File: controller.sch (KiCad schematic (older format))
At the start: 22 parts, among them J1 Conn_01x16, J2 Conn_01x08, J3 Conn_01x04, SW1 SW_Push, U1 PRTR5V0U2X, U2 AT90USB1286-AU, Y1 16MHz

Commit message: Rescue symbol
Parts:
- U2: symbol MCU_Microchip_AVR:AT90USB1286-AU -> controller-rescue:AT90USB1286-AU-MCU_Microchip_AVR
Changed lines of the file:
@@
 EESchema Schematic File Version 4
-LIBS:controller-cache
 EELAYER 30 0
 EELAYER END
@@
 	9700 4850 9500 4850
 $Comp
-L MCU_Microchip_AVR:AT90USB1286-AU U2
+L controller-rescue:AT90USB1286-AU-MCU_Microchip_AVR U2
 U 1 1 5DC2549C
 P 6750 3500

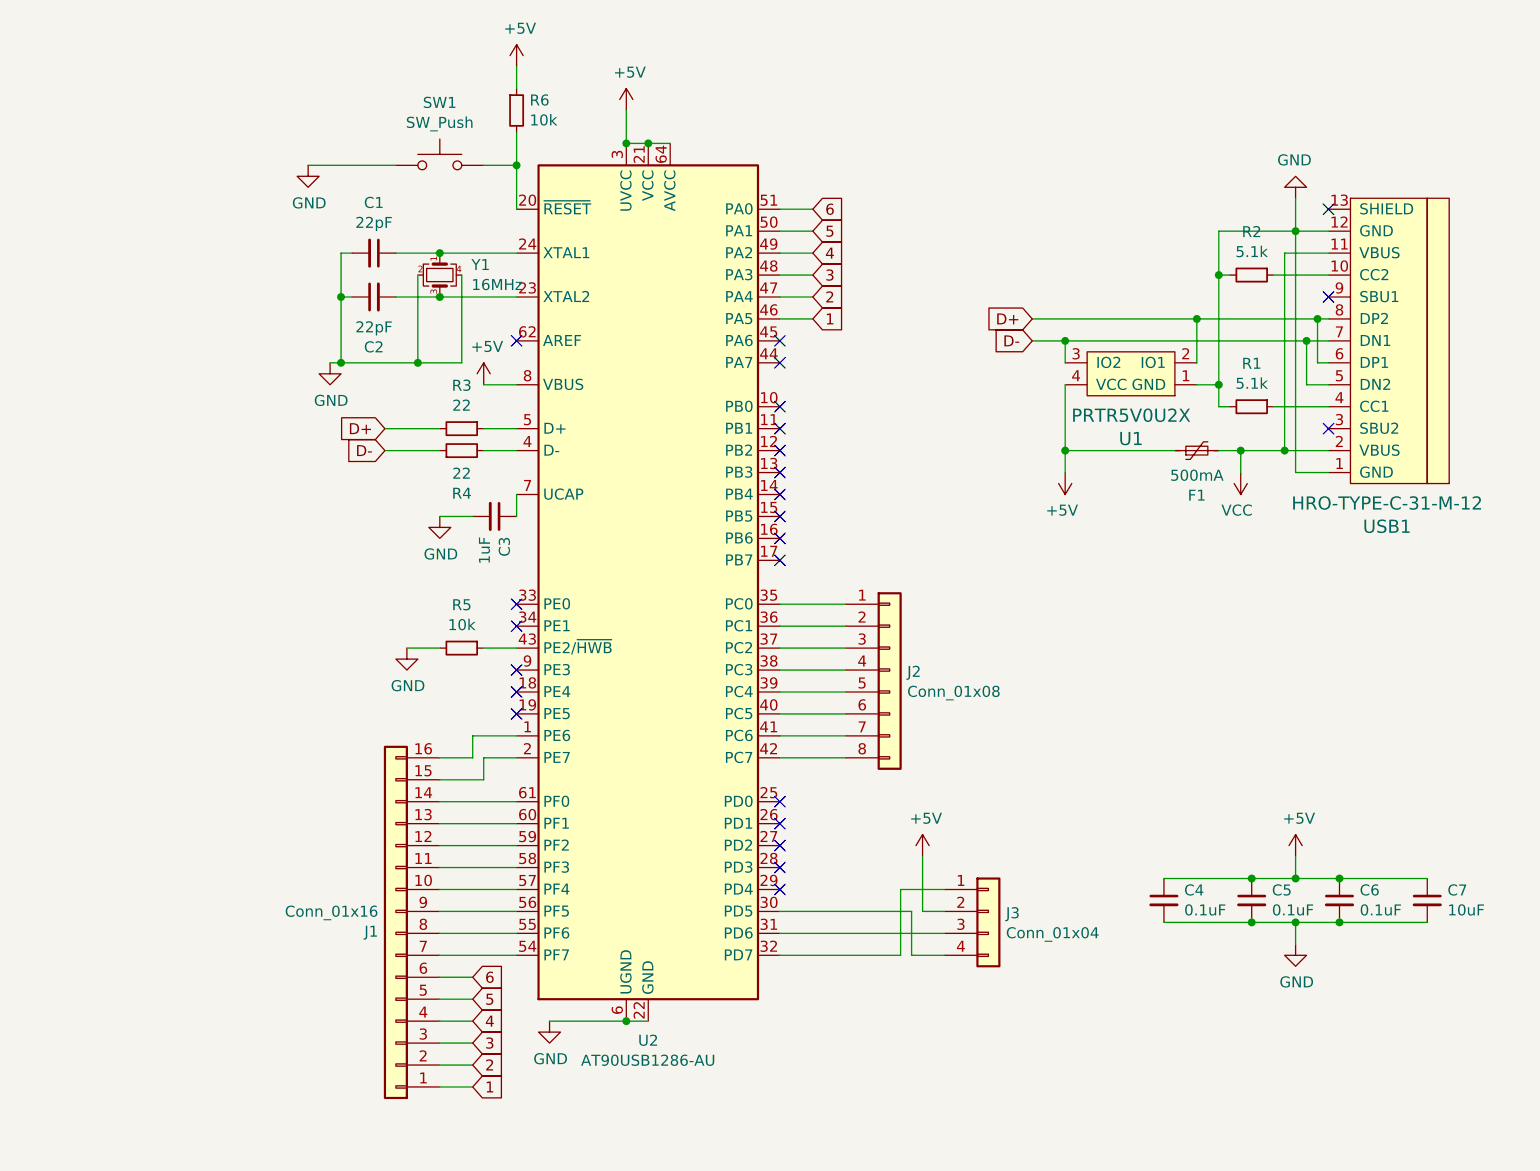
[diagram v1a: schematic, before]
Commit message: Schematic: add/delete/move connectors
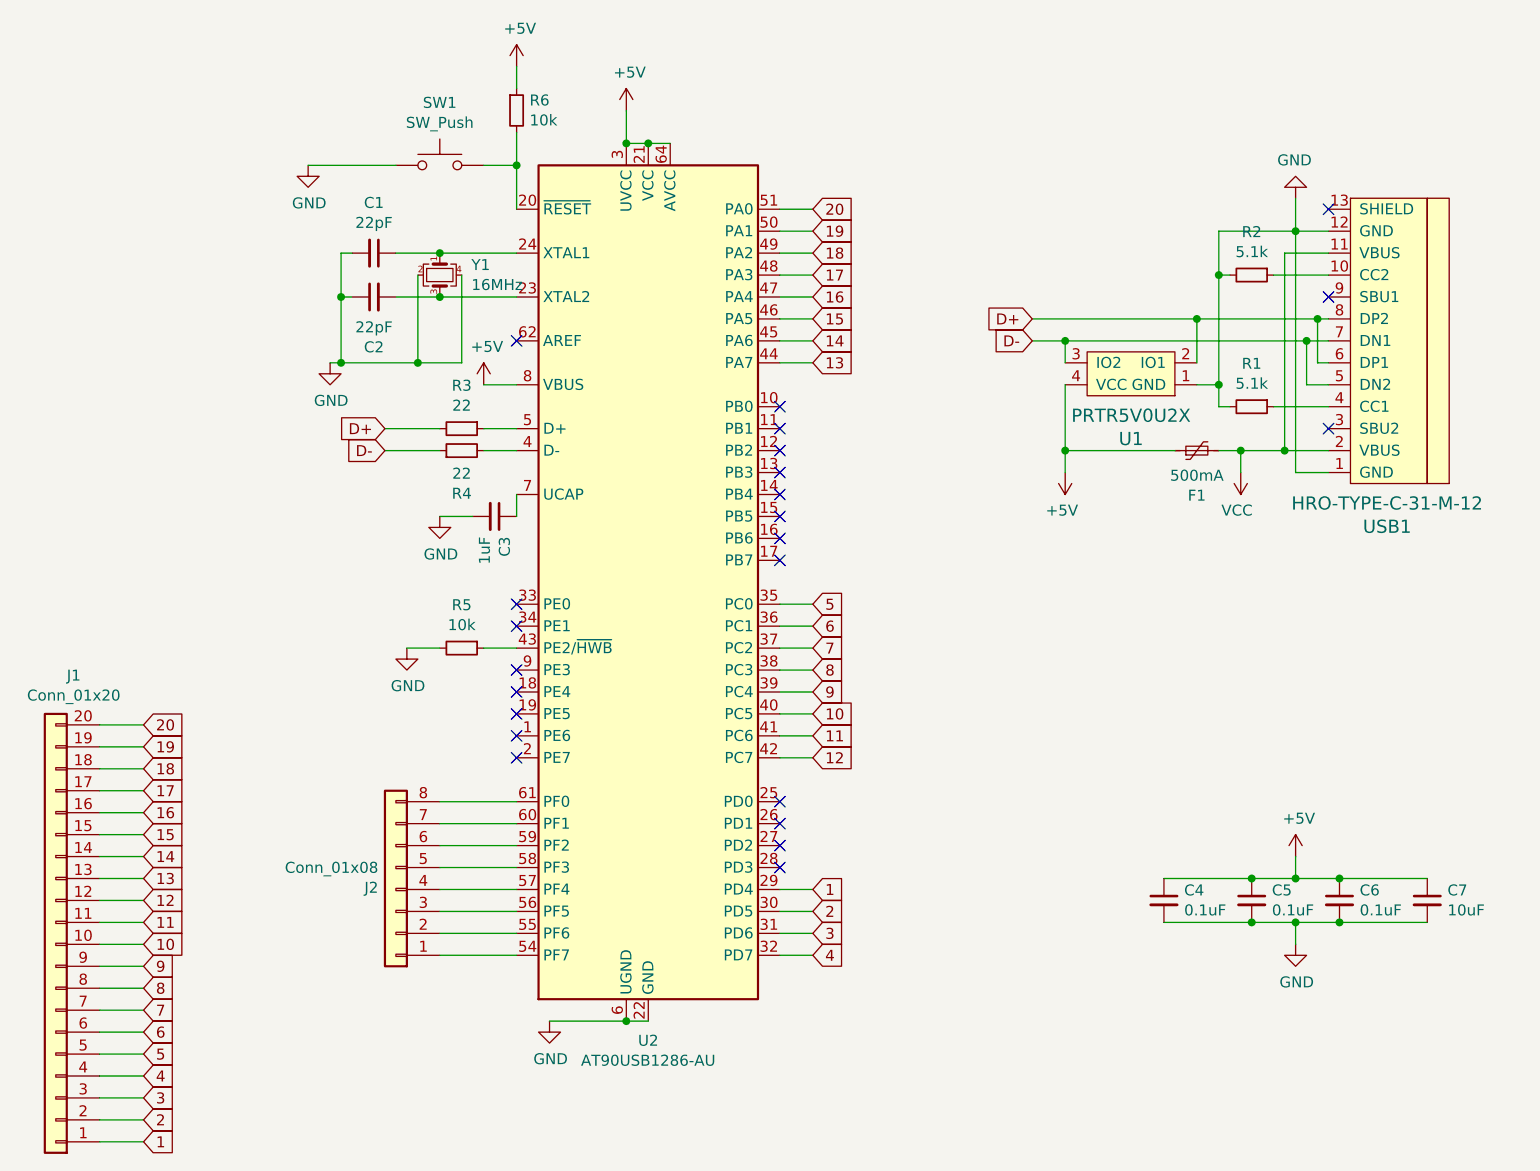
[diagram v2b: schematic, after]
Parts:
- removed J1: Conn_01x16, Connector_PinHeader_2.54mm:PinHeader_1x16_P2.54mm_Vertical, symbol Connector_Generic:Conn_01x16
- removed J3: Conn_01x04, Connector_PinHeader_2.54mm:PinHeader_1x04_P2.54mm_Vertical, symbol Connector_Generic:Conn_01x04
- added J1: Conn_01x20, symbol Connector_Generic:Conn_01x20
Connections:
- net 1: now also U2.29 (PD4), J1.1 (Pin_1); no longer U2.46 (PA5)
- net 2: now also U2.30 (PD5), J1.2 (Pin_2); no longer U2.47 (PA4)
- net 3: now also U2.31 (PD6), J1.3 (Pin_3); no longer U2.48 (PA3)
- net 4: now also U2.32 (PD7), J1.4 (Pin_4); no longer U2.49 (PA2)
- net 5: now also U2.35 (PC0), J1.5 (Pin_5); no longer U2.50 (PA1)
- net 6: now also U2.36 (PC1), J1.6 (Pin_6); no longer U2.51 (PA0)
- net at J2.1 (Pin_1): now also U2.54 (PF7); no longer U2.35 (PC0)
- net at J2.2 (Pin_2): now also U2.55 (PF6); no longer U2.36 (PC1)
- net at J2.3 (Pin_3): now also U2.56 (PF5); no longer U2.37 (PC2)
- net at J2.4 (Pin_4): now also U2.57 (PF4); no longer U2.38 (PC3)
- net at J2.5 (Pin_5): now also U2.58 (PF3); no longer U2.39 (PC4)
- net at J2.6 (Pin_6): now also U2.59 (PF2); no longer U2.40 (PC5)
- net at J2.7 (Pin_7): now also U2.60 (PF1); no longer U2.41 (PC6)
- net at J2.8 (Pin_8): now also U2.61 (PF0); no longer U2.42 (PC7)
- net 13: now reaches U2.44 (PA7)
- net 13: now also J1.13 (Pin_13)
- net 14: now reaches U2.45 (PA6)
- net 14: now also J1.14 (Pin_14)
- new net 10: J1.10 (Pin_10), U2.40 (PC5)
- new net 11: J1.11 (Pin_11), U2.41 (PC6)
- new net 12: J1.12 (Pin_12), U2.42 (PC7)
- new net 15: J1.15 (Pin_15), U2.46 (PA5)
- new net 16: J1.16 (Pin_16), U2.47 (PA4)
- new net 17: J1.17 (Pin_17), U2.48 (PA3)
- new net 18: J1.18 (Pin_18), U2.49 (PA2)
- new net 19: J1.19 (Pin_19), U2.50 (PA1)
- new net 20: J1.20 (Pin_20), U2.51 (PA0)
- new net 7: J1.7 (Pin_7), U2.37 (PC2)
- new net 8: J1.8 (Pin_8), U2.38 (PC3)
- new net 9: J1.9 (Pin_9), U2.39 (PC4)
- no-connect marks 24 -> 23
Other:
- moved on the sheet: J2
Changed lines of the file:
@@
 	6650 1350 6650 1500
 Connection ~ 6650 1500
-$Comp
-L power:+5V #PWR012
-U 1 1 5DD3F67F
-P 8000 4750
-F 0 "#PWR012" H 8000 4600 50  0001 C CNN
-F 1 "+5V" H 8015 4923 50  0000 C CNN
-F 2 "" H 8000 4750 50  0001 C CNN
-F 3 "" H 8000 4750 50  0001 C CNN
-	1    8000 4750
-	1    0    0    -1
-$EndComp
 NoConn ~ 6150 4100
 NoConn ~ 6150 4000
@@
 Wire Wire Line
 	9250 2300 8500 2300
-$Comp
-L Connector_Generic:Conn_01x08 J2
-U 1 1 5DD09096
-P 7850 3900
-F 0 "J2" H 7930 3892 50  0000 L CNN
-F 1 "Conn_01x08" H 7930 3801 50  0000 L CNN
-F 2 "Connector_PinHeader_2.54mm:PinHeader_1x08_P2.54mm_Vertical" H 7850 3900 50  0001 C CNN
-F 3 "~" H 7850 3900 50  0001 C CNN
-	1    7850 3900
-	1    0    0    -1
-$EndComp
-$Comp
-L Connector_Generic:Conn_01x16 J1
-U 1 1 5DD0A31D
-P 5600 5100
-F 0 "J1" H 5680 5092 50  0000 L CNN
-F 1 "Conn_01x16" H 5680 5001 50  0000 L CNN
-F 2 "Connector_PinHeader_2.54mm:PinHeader_1x16_P2.54mm_Vertical" H 5600 5100 50  0001 C CNN
-F 3 "~" H 5600 5100 50  0001 C CNN
-	1    5600 5100
-	-1   0    0    1
-$EndComp
-$Comp
-L Connector_Generic:Conn_01x04 J3
-U 1 1 5DD0B4D3
-P 8300 5000
-F 0 "J3" H 8380 4992 50  0000 L CNN
-F 1 "Conn_01x04" H 8380 4901 50  0000 L CNN
-F 2 "Connector_PinHeader_2.54mm:PinHeader_1x04_P2.54mm_Vertical" H 8300 5000 50  0001 C CNN
-F 3 "~" H 8300 5000 50  0001 C CNN
-	1    8300 5000
-	1    0    0    -1
-$EndComp
-Wire Wire Line
-	8100 5000 8000 5000
-Wire Wire Line
-	8000 5000 8000 4750
-Wire Wire Line
-	7350 3600 7650 3600
-Wire Wire Line
-	7350 3700 7650 3700
-Wire Wire Line
-	7650 3800 7350 3800
-Wire Wire Line
-	7350 3900 7650 3900
-Wire Wire Line
-	7650 4000 7350 4000
-Wire Wire Line
-	7350 4100 7650 4100
-Wire Wire Line
-	7650 4200 7350 4200
-Wire Wire Line
-	7350 4300 7650 4300
-Wire Wire Line
-	5800 4300 5950 4300
-Wire Wire Line
-	5950 4300 5950 4200
-Wire Wire Line
-	5950 4200 6150 4200
-Wire Wire Line
-	5800 4400 6000 4400
-Wire Wire Line
-	6000 4400 6000 4300
-Wire Wire Line
-	6000 4300 6150 4300
 Wire Wire Line
 	5800 4500 6150 4500
@@
 Wire Wire Line
 	6150 5200 5800 5200
-Text GLabel 5950 5300 2    50   Input ~ 0
-6
-Text GLabel 5950 5400 2    50   Input ~ 0
-5
-Text GLabel 5950 5500 2    50   Input ~ 0
-4
-Text GLabel 5950 5600 2    50   Input ~ 0
-3
-Text GLabel 5950 5700 2    50   Input ~ 0
-2
-Text GLabel 5950 5800 2    50   Input ~ 0
-1
-Wire Wire Line
-	5800 5800 5950 5800
-Wire Wire Line
-	5950 5700 5800 5700
-Wire Wire Line
-	5800 5600 5950 5600
-Wire Wire Line
-	5800 5500 5950 5500
-Wire Wire Line
-	5800 5400 5950 5400
-Wire Wire Line
-	5800 5300 5950 5300
 Text GLabel 7500 1800 2    50   Input ~ 0
-6
+20
 Text GLabel 7500 1900 2    50   Input ~ 0
-5
+19
 Text GLabel 7500 2000 2    50   Input ~ 0
-4
+18
 Text GLabel 7500 2100 2    50   Input ~ 0
-3
+17
 Text GLabel 7500 2200 2    50   Input ~ 0
-2
+16
 Text GLabel 7500 2300 2    50   Input ~ 0
-1
+15
 Wire Wire Line
 	7350 2300 7500 2300
@@
 	9700 1900 9700 1750
 NoConn ~ 9850 1800
-NoConn ~ 7350 4900
 NoConn ~ 7350 4800
 NoConn ~ 7350 4700
@@
 NoConn ~ 7350 2800
 NoConn ~ 7350 2700
-NoConn ~ 7350 2500
-NoConn ~ 7350 2400
 Wire Wire Line
 	9700 1900 9350 1900
@@
 	9350 1900 9350 2100
 Connection ~ 9350 2100
-Wire Wire Line
-	8100 5100 7350 5100
-Wire Wire Line
-	8100 5200 7950 5200
-Wire Wire Line
-	7950 5200 7950 5000
-Wire Wire Line
-	7950 5000 7350 5000
-Wire Wire Line
-	8100 4900 7900 4900
-Wire Wire Line
-	7900 4900 7900 5200
-Wire Wire Line
-	7900 5200 7350 5200
+$Comp
+L Connector_Generic:Conn_01x20 J1
+U 1 1 612A13B1
+P 4050 5150
+F 0 "J1" H 3968 3925 50  0000 C CNN
+F 1 "Conn_01x20" H 3968 4016 50  0000 C CNN
+F 2 "" H 4050 5150 50  0001 C CNN
+F 3 "~" H 4050 5150 50  0001 C CNN
+	1    4050 5150
+	-1   0    0    1
+$EndComp
+Text GLabel 4450 4150 2    50   Input ~ 0
+20
+Text GLabel 4450 4250 2    50   Input ~ 0
+19
+Text GLabel 4450 4350 2    50   Input ~ 0
+18
+Text GLabel 4450 4450 2    50   Input ~ 0
+17
+Text GLabel 4450 4550 2    50   Input ~ 0
+16
+Text GLabel 4450 4650 2    50   Input ~ 0
+15
+Text GLabel 4450 4750 2    50   Input ~ 0
+14
+Text GLabel 4450 4850 2    50   Input ~ 0
+13
+Text GLabel 4450 4950 2    50   Input ~ 0
+12
+Text GLabel 4450 5050 2    50   Input ~ 0
+11
+Text GLabel 4450 5150 2    50   Input ~ 0
+10
+Text GLabel 4450 5250 2    50   Input ~ 0
+9
+Text GLabel 4450 5350 2    50   Input ~ 0
+8
+Text GLabel 4450 5450 2    50   Input ~ 0
+7
+Text GLabel 4450 5550 2    50   Input ~ 0
+6
+Text GLabel 4450 5650 2    50   Input ~ 0
+5
+Text GLabel 4450 5750 2    50   Input ~ 0
+4
+Text GLabel 4450 5850 2    50   Input ~ 0
+3
+Text GLabel 4450 5950 2    50   Input ~ 0
+2
+Text GLabel 4450 6050 2    50   Input ~ 0
+1
+$Comp
+L Connector_Generic:Conn_01x08 J2
+U 1 1 5DD09096
+P 5600 4900
+F 0 "J2" H 5680 4892 50  0000 L CNN
+F 1 "Conn_01x08" H 5680 4801 50  0000 L CNN
+F 2 "Connector_PinHeader_2.54mm:PinHeader_1x08_P2.54mm_Vertical" H 5600 4900 50  0001 C CNN
+F 3 "~" H 5600 4900 50  0001 C CNN
+	1    5600 4900
+	-1   0    0    1
+$EndComp
+NoConn ~ 6150 4200
+NoConn ~ 6150 4300
+Text GLabel 7500 2400 2    50   Input ~ 0
+14
+Text GLabel 7500 2500 2    50   Input ~ 0
+13
+Wire Wire Line
+	7350 2400 7500 2400
+Wire Wire Line
+	7350 2500 7500 2500
+Wire Wire Line
+	4250 4150 4450 4150
+Wire Wire Line
+	4250 4250 4450 4250
+Wire Wire Line
+	4250 4350 4450 4350
+Wire Wire Line
+	4250 4450 4450 4450
+Wire Wire Line
+	4250 4550 4450 4550
+Wire Wire Line
+	4250 4650 4450 4650
+Wire Wire Line
+	4250 4750 4450 4750
+Wire Wire Line
+	4250 4850 4450 4850
+Wire Wire Line
+	4250 4950 4450 4950
+Wire Wire Line
+	4250 5050 4450 5050
+Wire Wire Line
+	4250 5150 4450 5150
+Wire Wire Line
+	4250 5250 4450 5250
+Wire Wire Line
+	4250 5350 4450 5350
+Wire Wire Line
+	4250 5450 4450 5450
+Wire Wire Line
+	4250 5550 4450 5550
+Wire Wire Line
+	4250 5650 4450 5650
+Wire Wire Line
+	4250 5750 4450 5750
+Wire Wire Line
+	4250 5850 4450 5850
+Wire Wire Line
+	4250 5950 4450 5950
+Wire Wire Line
+	4250 6050 4450 6050
+Text GLabel 7500 4300 2    50   Input ~ 0
+12
+Text GLabel 7500 4200 2    50   Input ~ 0
+11
+Text GLabel 7500 4100 2    50   Input ~ 0
+10
+Text GLabel 7500 4000 2    50   Input ~ 0
+9
+Text GLabel 7500 3900 2    50   Input ~ 0
+8
+Text GLabel 7500 3800 2    50   Input ~ 0
+7
+Text GLabel 7500 3700 2    50   Input ~ 0
+6
+Text GLabel 7500 3600 2    50   Input ~ 0
+5
+Text GLabel 7500 5200 2    50   Input ~ 0
+4
+Text GLabel 7500 5100 2    50   Input ~ 0
+3
+Text GLabel 7500 5000 2    50   Input ~ 0
+2
+Text GLabel 7500 4900 2    50   Input ~ 0
+1
+Wire Wire Line
+	7350 3600 7500 3600
+Wire Wire Line
+	7350 3700 7500 3700
+Wire Wire Line
+	7350 3800 7500 3800
+Wire Wire Line
+	7350 3900 7500 3900
+Wire Wire Line
+	7350 4000 7500 4000
+Wire Wire Line
+	7350 4100 7500 4100
+Wire Wire Line
+	7350 4200 7500 4200
+Wire Wire Line
+	7350 4300 7500 4300
+Wire Wire Line
+	7350 4900 7500 4900
+Wire Wire Line
+	7350 5000 7500 5000
+Wire Wire Line
+	7350 5100 7500 5100
+Wire Wire Line
+	7350 5200 7500 5200
 $EndSCHEMATC
